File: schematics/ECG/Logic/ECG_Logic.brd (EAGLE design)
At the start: 30.1 x 26.7 mm, 76 parts, among them IC1 ADS1293, IC2 LIS3DH, IC3 MCP1703, IC4 CC2541, IC5 FSA4157, IC6 FSA4157, IC7 FSA4157, IC9 LTC6907, X1 XTAL-2SMD, X2 XTAL_403

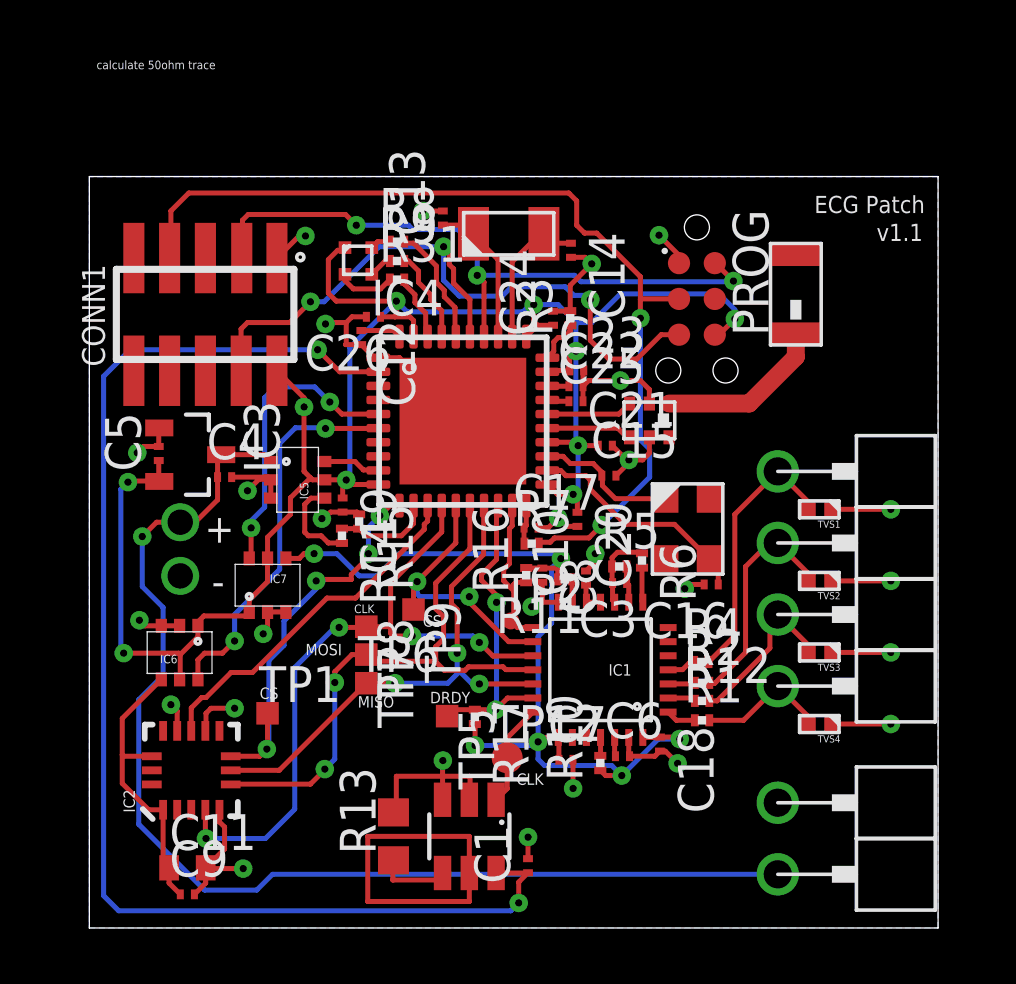
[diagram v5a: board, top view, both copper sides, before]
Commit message: added analog switch to OSC. OSC resistor changed to 500K ohm for 400KHz operation
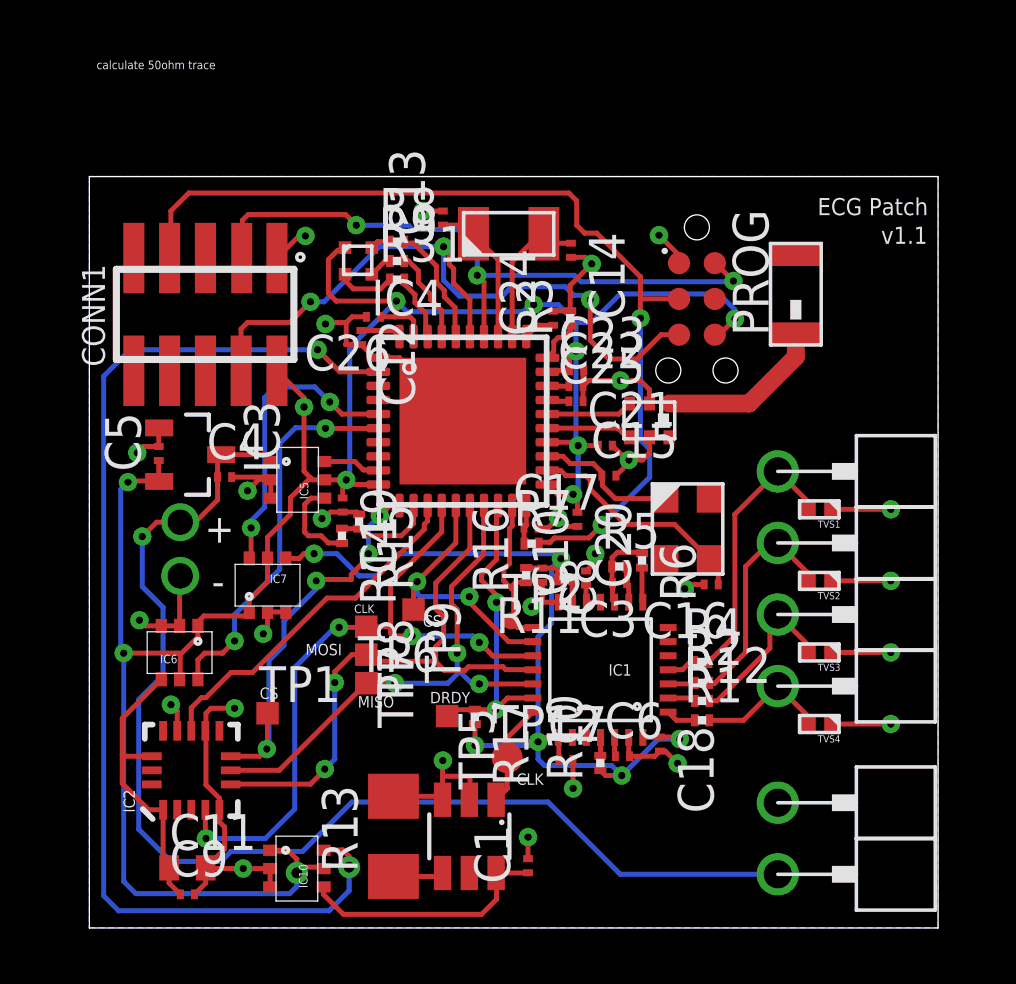
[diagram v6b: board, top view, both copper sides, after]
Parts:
- added IC10: FSA4157, fairchild:SC70-6
- R13: value 50K -> 500K; device rcl:R0603 -> rcl:R1206
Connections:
- removed net ADS1293_RESET: IC4.7
- removed net ADS1923_OSC_VCC: C1.1, IC4.2, IC9.6
- new net OSC_SW_VCC: IC10.6, IC4.2
- new net OSC_VCC: C1.1, IC10.4, IC9.6
- net GND: now also IC10.2, IC10.3
- net VCC: now also IC10.1, IC10.5
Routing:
- net ADS1923_OSC_VCC: track 46.3 -> 0.00 mm, vias 2 -> 0
- net OSC_SW_VCC: track 0.00 -> 40.4 mm, vias 0 -> 2
- net VCC: track 72.0 -> 89.8 mm, vias 10 -> 11
- net GRD: track 11.8 -> 0.00 mm
- net OSC_VCC: track 0.00 -> 9.00 mm
- net GND: track 62.9 -> 68.1 mm
- net BATT: track 41.5 -> 42.9 mm
- net N$14: track 2.74 -> 2.04 mm

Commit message: added board detect pin, need to find proper place to route trace
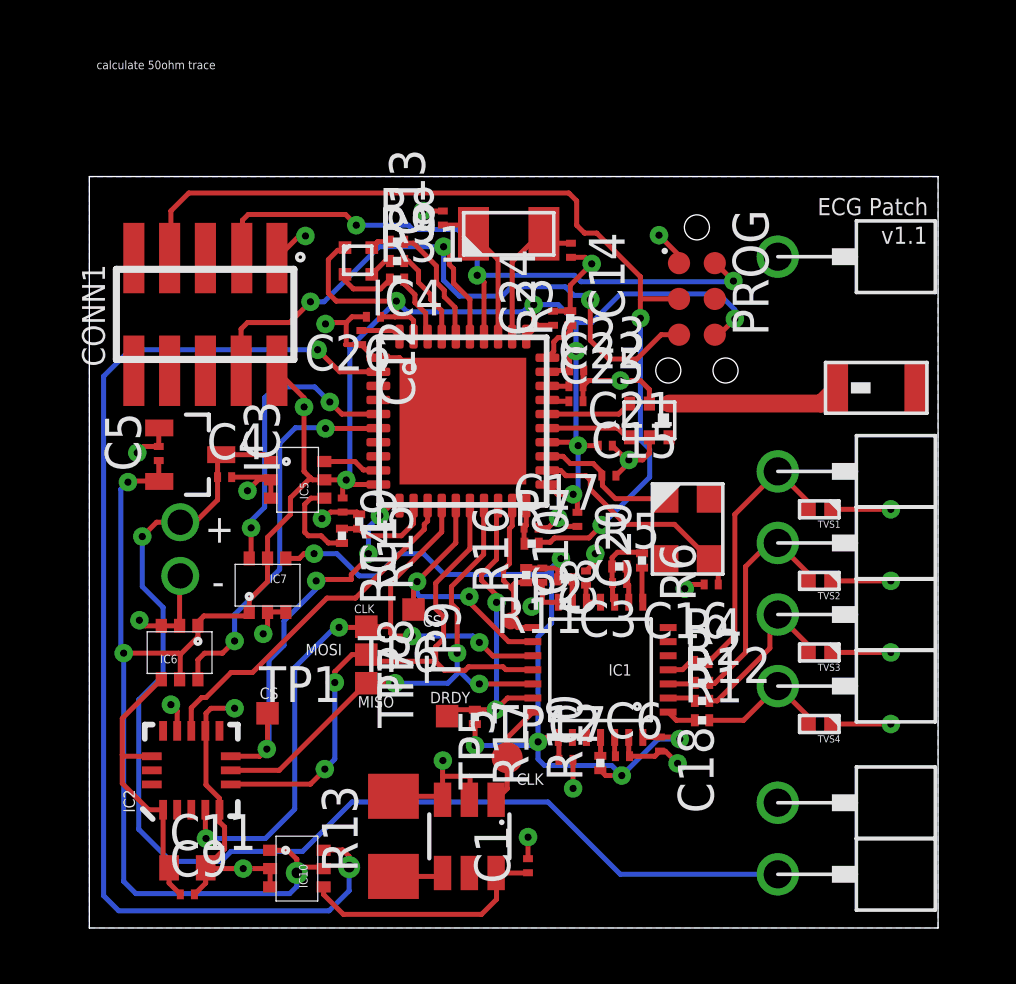
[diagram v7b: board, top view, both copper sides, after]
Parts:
- added U$7: TARGET_RA, pins:TARGET_RA
- moved RF 4.49 mm to (28.0, 19.2), turned to 180 degrees
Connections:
- new net BOARD_DETECT: U$7.1
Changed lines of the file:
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@@
 <text x="6.0452" y="8.128" size="0.4064" layer="21">CS</text>
 <text x="11.8364" y="10.6934" size="0.4064" layer="21">CS</text>
-<text x="0.254" y="28.1432" size="0.3048" layer="48">removed X3,C1,C2</text>
+<text x="0.2286" y="29.1592" size="0.3048" layer="48">removed X3,C1,C2</text>
 <text x="0.254" y="29.7688" size="0.3048" layer="48">Added LTC6907 , C1, and R13 (PNM0603E5002BST5)</text>
 <text x="0.254" y="30.48" size="0.3048" layer="21">calculate 50ohm trace</text>
@@
 <element name="TVS3" library="semtech" package="0402" value="ZD_0402" x="25.908" y="9.779" rot="R180"/>
 <element name="TVS4" library="semtech" package="0402" value="ZD_0402" x="25.908" y="7.239" rot="R180"/>
-<element name="RF" library="johanson" package="ANTENNA_SMD" value="ANTENNA_SMD" x="25.0756" y="22.5698" rot="R270"/>
+<element name="RF" library="johanson" package="ANTENNA_SMD" value="ANTENNA_SMD" x="28.0054" y="19.1712" rot="R180"/>
 <element name="IC8" library="johanson" package="BALUN_SMD_2450BM_SERIES" value="" x="19.812" y="17.9832"/>
 <element name="PROG" library="tagconnect" package="TC2030-MCP-NL" value="TC2030-MCP-NL" x="21.5646" y="24.8666" rot="R270"/>
@@
 <element name="U$6" library="pins" package="TARGET_RA" value="TARGET_RA" x="24.4348" y="1.905"/>
 <element name="IC10" library="fairchild" package="SC70-6" value="FSA4157" x="7.366" y="2.0574" rot="R270"/>
+<element name="U$7" library="pins" package="TARGET_RA" value="TARGET_RA" x="24.4348" y="23.8252"/>
 </elements>
 <signals>
@@
 <wire x1="9.5758" y1="12.4968" x2="10.2108" y2="12.4968" width="0.1778" layer="16"/>
 <wire x1="10.2108" y1="12.4968" x2="10.9982" y2="13.2842" width="0.1778" layer="16"/>
-<wire x1="10.9982" y1="13.2842" x2="16.5608" y2="13.2842" width="0.1778" layer="16"/>
-<wire x1="16.5608" y1="13.2842" x2="16.7386" y2="13.1064" width="0.1778" layer="16"/>
 <via x="13.6906" y="6.477" extent="1-16" drill="0.254"/>
 <wire x1="16.6664" y1="5.969" x2="16.6664" y2="6.7398" width="0.1778" layer="1"/>
@@
 <wire x1="13.6906" y1="6.477" x2="13.6906" y2="7.2294" width="0.1778" layer="1"/>
 <wire x1="13.6906" y1="7.2294" x2="13.6824" y2="7.2376" width="0.1778" layer="1"/>
+<wire x1="10.9982" y1="13.2842" x2="11.8618" y2="13.2842" width="0.1778" layer="16"/>
+<wire x1="11.8618" y1="13.2842" x2="12.5984" y2="12.5476" width="0.1778" layer="16"/>
+<wire x1="12.5984" y1="12.5476" x2="16.1798" y2="12.5476" width="0.1778" layer="16"/>
+<wire x1="16.1798" y1="12.5476" x2="16.7386" y2="13.1064" width="0.1778" layer="16"/>
 </signal>
 <signal name="BLUE_LED">
@@
 <contactref element="IC8" pad="1"/>
 <contactref element="RF" pad="1"/>
-<wire x1="20.577" y1="18.6142" x2="23.42" y2="18.6142" width="0.635" layer="1"/>
-<wire x1="25.0756" y1="21.0938" x2="25.0756" y2="20.2698" width="0.635" layer="1"/>
-<wire x1="25.0756" y1="20.2698" x2="23.42" y2="18.6142" width="0.635" layer="1"/>
+<wire x1="20.577" y1="18.6142" x2="25.9724" y2="18.6142" width="0.635" layer="1"/>
+<wire x1="25.9724" y1="18.6142" x2="26.5294" y2="19.1712" width="0.635" layer="1"/>
 </signal>
 <signal name="N/C">
@@
 <wire x1="8.316" y1="1.4574" x2="8.316" y2="1.1836" width="0.1778" layer="1"/>
 </signal>
+<signal name="BOARD_DETECT">
+<contactref element="U$7" pad="1"/>
+</signal>
 </signals>

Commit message: routed detect pin to cc2541
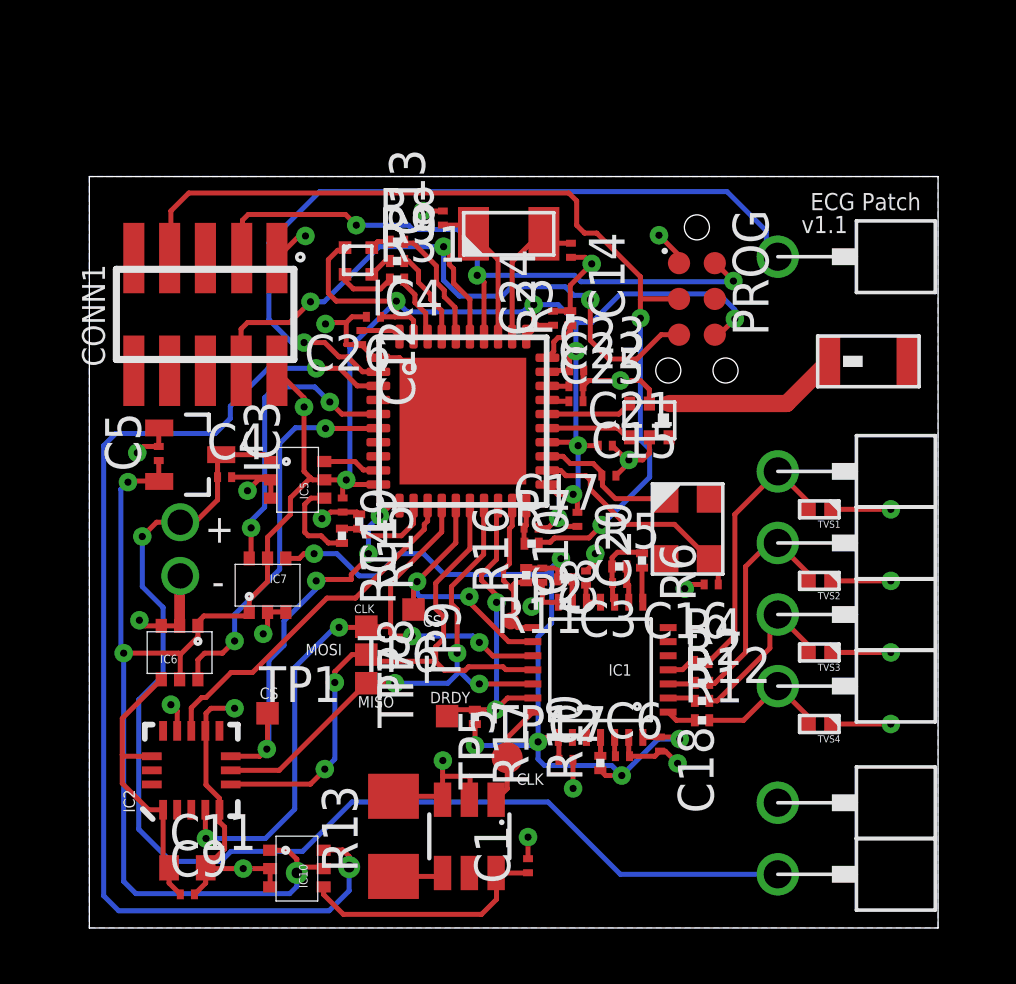
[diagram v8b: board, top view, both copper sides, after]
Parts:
- moved RF 0.98 mm to (27.7, 20.1)
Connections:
- net BOARD_DETECT: now also IC4.2
- net OSC_SW_VCC: now also IC4.3; no longer IC4.2
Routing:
- net BOARD_DETECT: track 0.00 -> 27.5 mm, vias 0 -> 1
- net OSC_SW_VCC: track 40.4 -> 38.8 mm
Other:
- board text removed: "calculate 50ohm trace"
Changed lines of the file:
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@@
 <?xml version="1.0" encoding="utf-8"?>
 <!DOCTYPE eagle SYSTEM "eagle.dtd">
-<eagle version="6.4">
+<eagle version="6.5.0">
 <drawing>
 <settings>
@@
 <wire x1="30.1244" y1="26.67" x2="0" y2="26.67" width="0" layer="20"/>
 <wire x1="0" y1="26.67" x2="0" y2="0" width="0" layer="20"/>
-<text x="29.7688" y="25.908" size="0.6096" layer="21" rot="R180">ECG Patch</text>
-<text x="29.7434" y="24.892" size="0.6096" layer="21" rot="R180">v1.1</text>
+<text x="29.5148" y="26.0858" size="0.6096" layer="21" rot="R180">ECG Patch</text>
+<text x="25.273" y="24.6634" size="0.6096" layer="21">v1.1</text>
 <text x="9.525" y="7.8232" size="0.4064" layer="21">MISO</text>
 <text x="7.6708" y="9.6774" size="0.4064" layer="21">MOSI</text>
@@
 <text x="0.2286" y="29.1592" size="0.3048" layer="48">removed X3,C1,C2</text>
 <text x="0.254" y="29.7688" size="0.3048" layer="48">Added LTC6907 , C1, and R13 (PNM0603E5002BST5)</text>
-<text x="0.254" y="30.48" size="0.3048" layer="21">calculate 50ohm trace</text>
 <text x="4.0938" y="13.6746" size="1.016" layer="21">+</text>
 <text x="4.3446" y="11.8" size="1.016" layer="21">-</text>
@@
 <element name="TVS3" library="semtech" package="0402" value="ZD_0402" x="25.908" y="9.779" rot="R180"/>
 <element name="TVS4" library="semtech" package="0402" value="ZD_0402" x="25.908" y="7.239" rot="R180"/>
-<element name="RF" library="johanson" package="ANTENNA_SMD" value="ANTENNA_SMD" x="28.0054" y="19.1712" rot="R180"/>
+<element name="RF" library="johanson" package="ANTENNA_SMD" value="ANTENNA_SMD" x="27.726" y="20.111" rot="R180"/>
 <element name="IC8" library="johanson" package="BALUN_SMD_2450BM_SERIES" value="" x="19.812" y="17.9832"/>
 <element name="PROG" library="tagconnect" package="TC2030-MCP-NL" value="TC2030-MCP-NL" x="21.5646" y="24.8666" rot="R270"/>
@@
 <wire x1="5.461" y1="2.1082" x2="6.4152" y2="2.1082" width="0.1778" layer="1"/>
 <wire x1="6.4152" y1="2.1082" x2="6.416" y2="2.1074" width="0.1778" layer="1"/>
-<wire x1="3.2036" y1="10.7234" x2="3.2036" y2="12.4746" width="0.1778" layer="1"/>
+<wire x1="3.2036" y1="10.7234" x2="3.2036" y2="12.4746" width="0.381" layer="1"/>
 <wire x1="3.2036" y1="12.4746" x2="3.2258" y2="12.4968" width="0.1778" layer="1"/>
 <wire x1="10.795" y1="4.6732" x2="12.4154" y2="4.6732" width="0.1778" layer="1"/>
@@
 <contactref element="IC8" pad="1"/>
 <contactref element="RF" pad="1"/>
-<wire x1="20.577" y1="18.6142" x2="25.9724" y2="18.6142" width="0.635" layer="1"/>
-<wire x1="25.9724" y1="18.6142" x2="26.5294" y2="19.1712" width="0.635" layer="1"/>
+<wire x1="20.577" y1="18.6142" x2="24.7532" y2="18.6142" width="0.6096" layer="1"/>
+<wire x1="24.7532" y1="18.6142" x2="26.25" y2="20.111" width="0.6096" layer="1"/>
 </signal>
 <signal name="N/C">
@@
 </signal>
 <signal name="OSC_SW_VCC">
-<contactref element="IC4" pad="2"/>
-<via x="8.1026" y="20.5232" extent="1-16" drill="0.254"/>
-<wire x1="0.508" y1="19.5834" x2="0.508" y2="1.143" width="0.1778" layer="16"/>
+<wire x1="0.508" y1="17.1196" x2="0.508" y2="1.143" width="0.1778" layer="16"/>
 <wire x1="0.508" y1="1.143" x2="1.0414" y2="0.6096" width="0.1778" layer="16"/>
-<wire x1="8.1026" y1="20.5232" x2="1.4478" y2="20.5232" width="0.1778" layer="16"/>
-<wire x1="1.4478" y1="20.5232" x2="0.508" y2="19.5834" width="0.1778" layer="16"/>
-<wire x1="10.2578" y1="19.74" x2="8.8858" y2="19.74" width="0.1778" layer="1"/>
-<wire x1="8.8858" y1="19.74" x2="8.1026" y2="20.5232" width="0.1778" layer="1"/>
 <contactref element="IC10" pad="6"/>
 <wire x1="1.0414" y1="0.6096" x2="8.509" y2="0.6096" width="0.1778" layer="16"/>
@@
 <wire x1="8.9916" y1="2.7686" x2="8.3272" y2="2.7686" width="0.1778" layer="1"/>
 <wire x1="8.3272" y1="2.7686" x2="8.316" y2="2.7574" width="0.1778" layer="1"/>
+<contactref element="IC4" pad="3"/>
+<wire x1="10.2578" y1="19.24" x2="9.5128" y2="19.24" width="0.1778" layer="1"/>
+<wire x1="9.5128" y1="19.24" x2="8.89" y2="19.8628" width="0.1778" layer="1"/>
+<wire x1="8.89" y1="19.8628" x2="8.0518" y2="19.8628" width="0.1778" layer="1"/>
+<via x="8.0518" y="19.8628" extent="1-16" drill="0.254"/>
+<wire x1="8.0518" y1="19.8628" x2="6.35" y2="19.8628" width="0.1778" layer="16"/>
+<wire x1="6.35" y1="19.8628" x2="5.0038" y2="18.5166" width="0.1778" layer="16"/>
+<wire x1="5.0038" y1="18.5166" x2="5.0038" y2="18.0848" width="0.1778" layer="16"/>
+<wire x1="5.0038" y1="18.0848" x2="4.4704" y2="17.5514" width="0.1778" layer="16"/>
+<wire x1="4.4704" y1="17.5514" x2="0.9398" y2="17.5514" width="0.1778" layer="16"/>
+<wire x1="0.9398" y1="17.5514" x2="0.508" y2="17.1196" width="0.1778" layer="16"/>
 </signal>
 <signal name="OSC_VCC">
@@
 <signal name="BOARD_DETECT">
 <contactref element="U$7" pad="1"/>
+<contactref element="IC4" pad="2"/>
+<wire x1="10.2578" y1="19.74" x2="9.6986" y2="19.74" width="0.1778" layer="1"/>
+<wire x1="9.6986" y1="19.74" x2="9.1694" y2="20.2692" width="0.1778" layer="1"/>
+<wire x1="9.1694" y1="20.2692" x2="8.8646" y2="20.2692" width="0.1778" layer="1"/>
+<wire x1="8.8646" y1="20.2692" x2="8.3566" y2="20.7772" width="0.1778" layer="1"/>
+<wire x1="8.3566" y1="20.7772" x2="7.62" y2="20.7772" width="0.1778" layer="1"/>
+<via x="7.62" y="20.7772" extent="1-16" drill="0.254"/>
+<wire x1="7.62" y1="20.7772" x2="7.1882" y2="20.7772" width="0.1778" layer="16"/>
+<wire x1="7.1882" y1="20.7772" x2="6.3754" y2="21.59" width="0.1778" layer="16"/>
+<wire x1="6.3754" y1="21.59" x2="6.3754" y2="24.3332" width="0.1778" layer="16"/>
+<wire x1="6.3754" y1="24.3332" x2="8.1788" y2="26.1366" width="0.1778" layer="16"/>
+<wire x1="8.1788" y1="26.1366" x2="22.6314" y2="26.1366" width="0.1778" layer="16"/>
+<wire x1="22.6314" y1="26.1366" x2="24.0284" y2="24.7396" width="0.1778" layer="16"/>
+<wire x1="24.0284" y1="24.7396" x2="24.0284" y2="24.2316" width="0.1778" layer="16"/>
+<wire x1="24.0284" y1="24.2316" x2="24.4348" y2="23.8252" width="0.1778" layer="16"/>
 </signal>
 </signals>
